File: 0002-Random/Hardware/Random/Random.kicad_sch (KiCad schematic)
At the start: 11 parts, among them J1 OUT_INV, J2 OUT, J3 OUT_HALF, U1 ATtiny85-20S

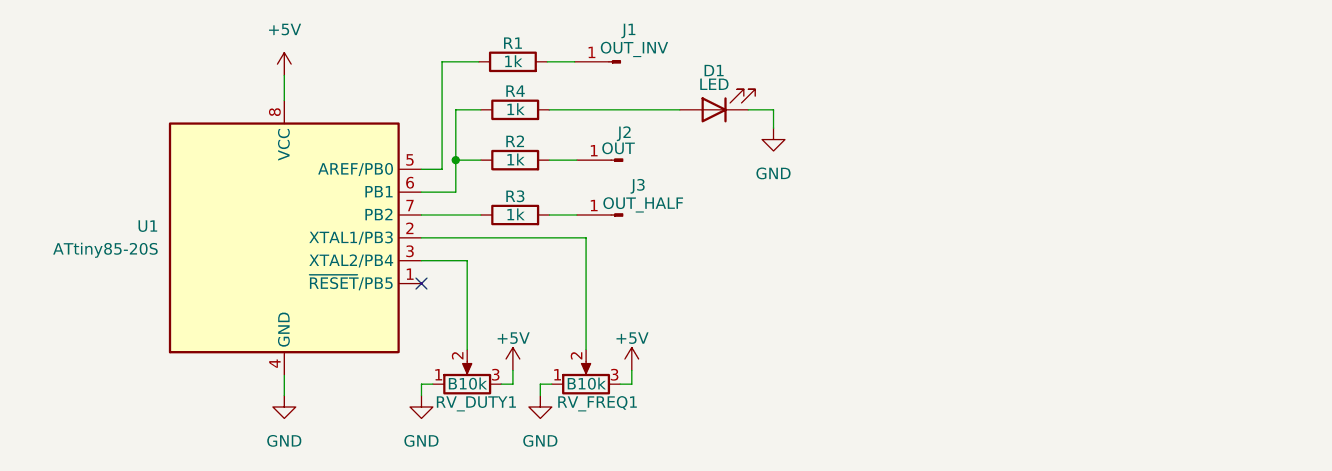
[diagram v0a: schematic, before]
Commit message: Added schematics for Random
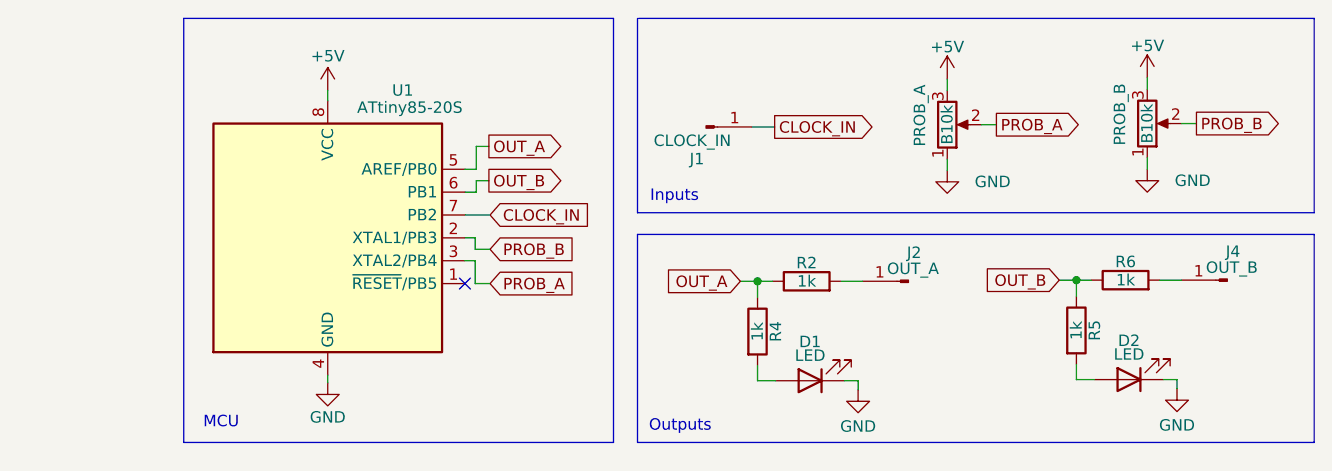
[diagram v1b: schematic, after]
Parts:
- removed J3: OUT_HALF, symbol Connector:Conn_01x01_Pin
- removed R1, R3: 1k, symbol Device:R
- removed RV_FREQ1: B10k, symbol Device:R_Potentiometer
- added D2: LED, symbol Device:LED
- added J4: OUT_B, symbol Connector:Conn_01x01_Pin
- added PROB_B: B10k, symbol Device:R_Potentiometer
- added R5, R6: 1k, symbol Device:R
- J1: value OUT_INV -> CLOCK_IN
- J2: value OUT -> OUT_A
- renumbered RV_DUTY1 to PROB_A
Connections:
- net +5V: now also PROB_B.3
- net GND: now also D2.1 (K), PROB_B.1
- net CLOCK_IN: now reaches U1.7 (PB2)
- net CLOCK_IN: now also J1.1 (Pin_1)
- net PROB_B: now reaches U1.2 (XTAL1/PB3)
- net PROB_B: now also PROB_B.2
- net PROB_A: now reaches PROB_A.2, U1.3 (XTAL2/PB4)
- net OUT_A: now reaches U1.5 (AREF/PB0)
- net OUT_A: now also R2.1, R4.1
- new net: J4.1 (Pin_1), R6.2
- new net: D2.2 (A), R5.2
- new net OUT_B: R5.1, R6.1, U1.6 (PB1)
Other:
- note added: "Inputs"
- note added: "MCU"
- note added: "Outputs"
- moved on the sheet: D1, J1, J2, PROB_A, R2, U1
